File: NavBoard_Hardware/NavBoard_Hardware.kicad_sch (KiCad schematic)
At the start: 0 parts

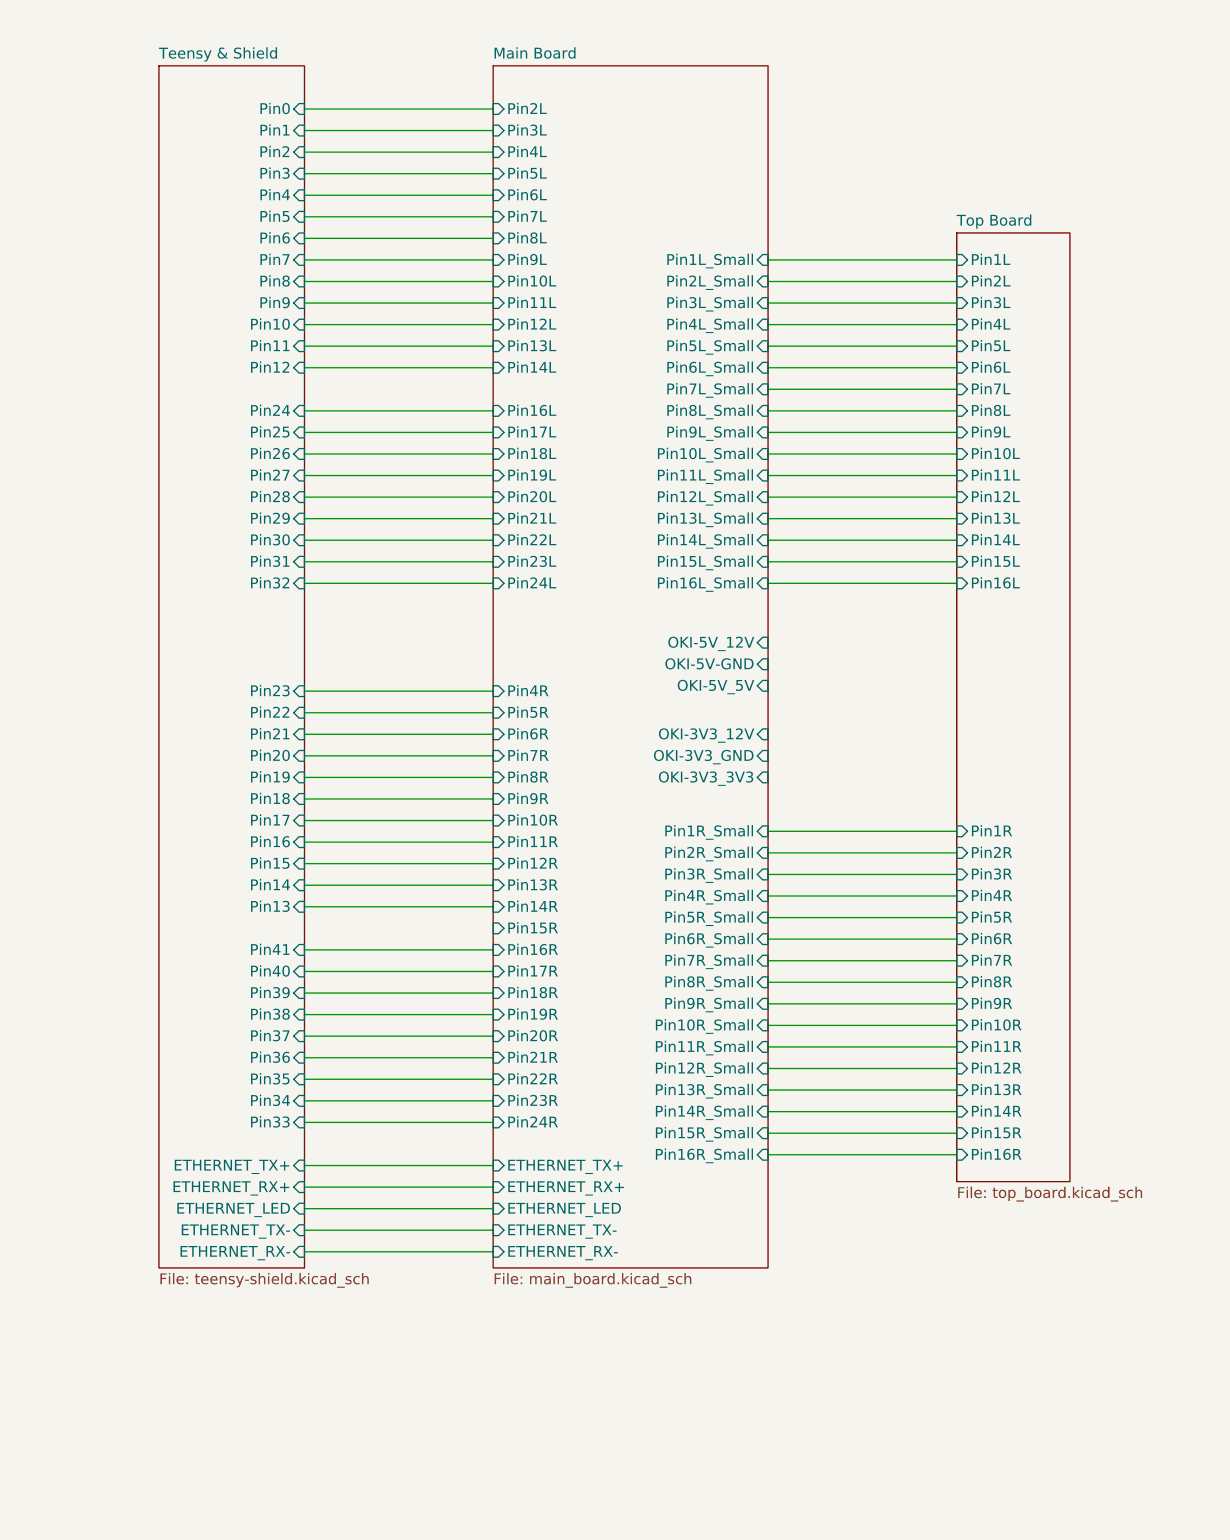
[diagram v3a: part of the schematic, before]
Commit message: Most schematic connections completed
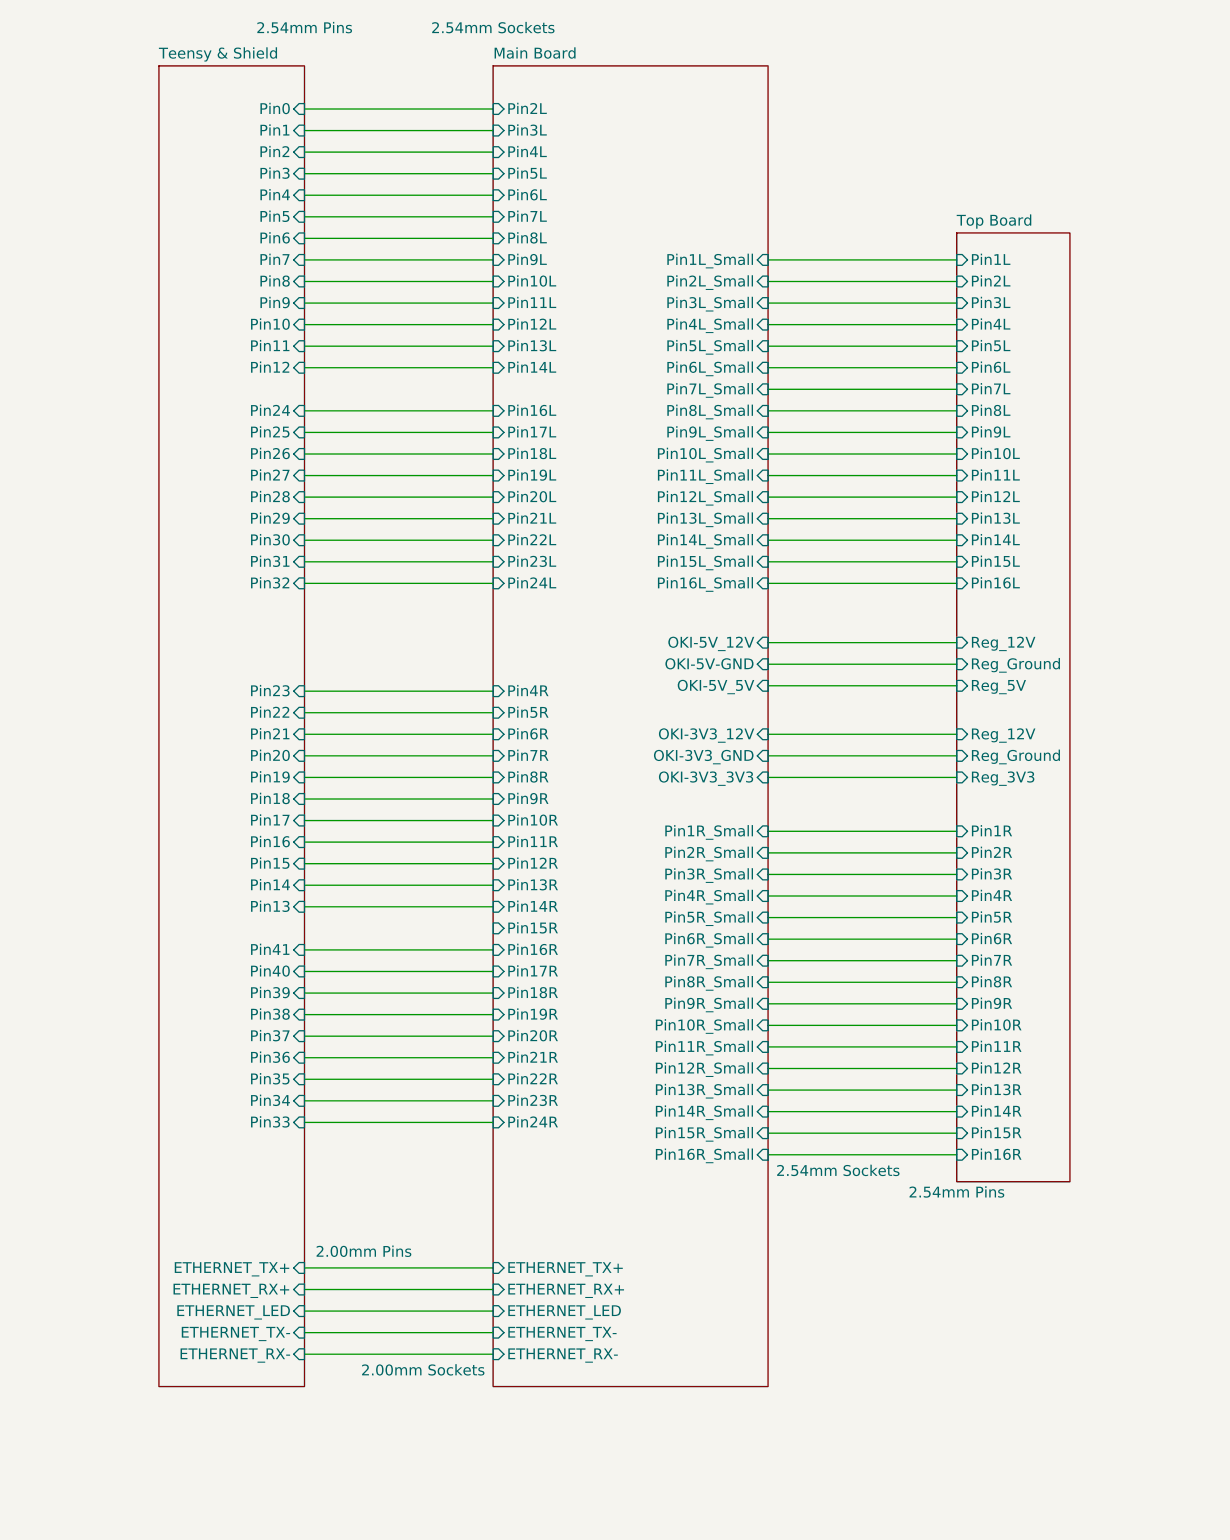
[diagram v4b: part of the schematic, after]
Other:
- sheet Top Board ports: added Reg_12V, Reg_3V3, Reg_5V, Reg_Ground; removed none

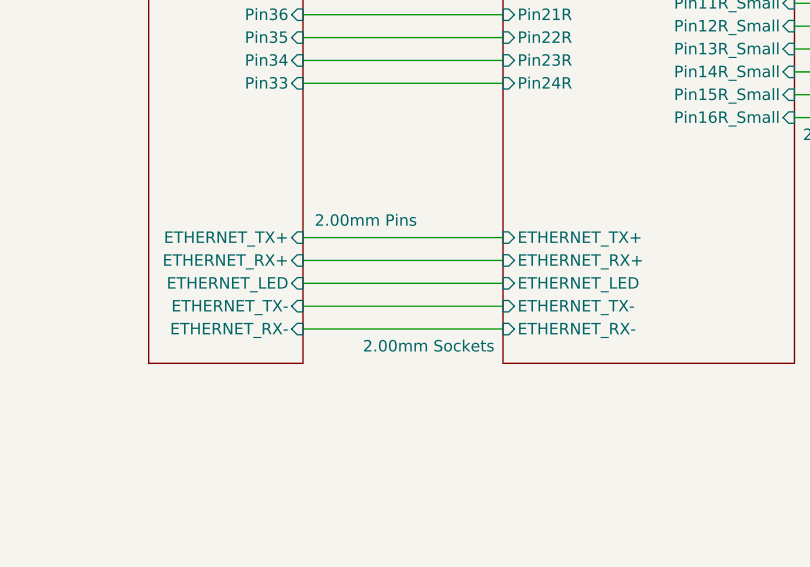
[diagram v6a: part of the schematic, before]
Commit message: Resized Ethernet to 2.54mm
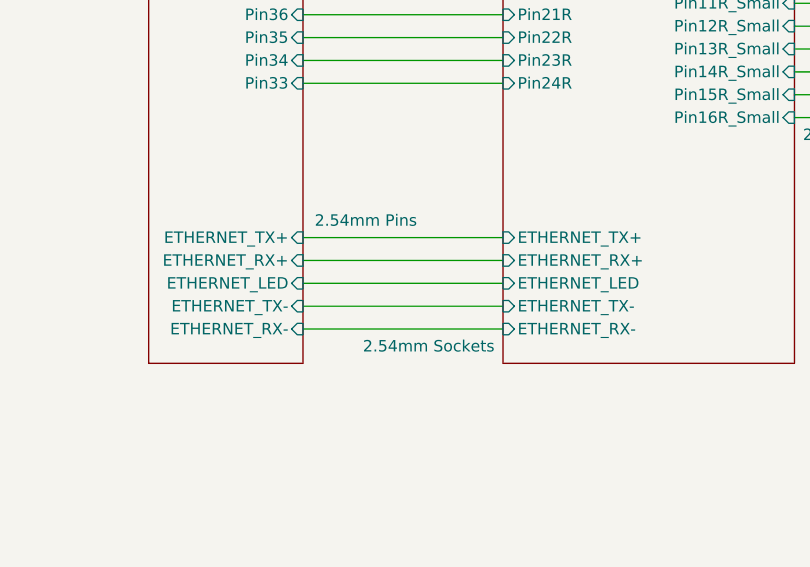
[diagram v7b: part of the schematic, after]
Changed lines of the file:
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@@
     )
     (property "Header Type" "2.54mm Sockets" (id 2) (at 118.11 21.59 0))
-    (property "Ethernet Header Type" "2.00mm Sockets" (id 3) (at 109.855 179.705 0))
+    (property "Ethernet Header Type" "2.54mm Sockets" (id 3) (at 109.855 179.705 0))
     (property "Inner Header Type" "2.54mm Sockets" (id 4) (at 158.75 156.21 0))
     (pin "ETHERNET_LED" input (at 118.11 172.72 180)
@@
     )
     (property "Header Type" "2.54mm Pins" (id 2) (at 95.885 21.59 0))
-    (property "Ethernet Header Type" "2.00mm Pins" (id 3) (at 102.87 165.735 0))
+    (property "Ethernet Header Type" "2.54mm Pins" (id 3) (at 102.87 165.735 0))
     (pin "ETHERNET_RX-" input (at 95.885 177.8 0)
       (effects (font (size 1.27 1.27)) (justify right))
@@
       (reference "#PWR047") (unit 1) (value "GND") (footprint "")
     )
+    (path "/f643fe13-52b3-46d1-8243-a8bbe65cd5c3/19d38986-c68b-4a05-8050-ecac7441163e"
+      (reference "#PWR?") (unit 1) (value "GND") (footprint "")
+    )
     (path "/1cf30331-e31a-4dae-8418-1a281b51585f/cfa695dc-e859-4ad7-a02d-ada1f7512f16/d997983e-985b-4240-8c4e-c57a43eedad7"
       (reference "C1") (unit 1) (value "0.1uF") (footprint "Capacitor_SMD:C_0603_1608Metric_Pad1.08x0.95mm_HandSolder")
@@
     )
     (path "/40b46045-12d0-4208-984c-573a30ffe5b1/837c6c65-a505-4a3a-b098-3f51addddc5f"
-      (reference "J2") (unit 1) (value "Teensy Ethernet") (footprint "Connector_PinSocket_2.00mm:PinSocket_2x03_P2.00mm_Vertical")
+      (reference "J2") (unit 1) (value "Teensy Ethernet") (footprint "Connector_PinSocket_2.54mm:PinSocket_2x03_P2.54mm_Vertical")
     )
     (path "/40b46045-12d0-4208-984c-573a30ffe5b1/7ad0c62d-6820-4583-8e6c-b98466a24e10"
@@
       (reference "J8") (unit 1) (value "6 Pin Molex Micro-Fit") (footprint "Connector_Molex:Molex_Micro-Fit_3.0_43650-0600_1x06_P3.00mm_Horizontal")
     )
+    (path "/f643fe13-52b3-46d1-8243-a8bbe65cd5c3/44c5f4fd-8f37-434e-a7f1-2821029d5e51"
+      (reference "J?") (unit 1) (value "Teensy Ethernet") (footprint "Connector_PinSocket_2.00mm:PinSocket_2x03_P2.00mm_Vertical")
+    )
     (path "/1cf30331-e31a-4dae-8418-1a281b51585f/fc5a0194-7f1f-41ed-a352-74d1778bc892"
